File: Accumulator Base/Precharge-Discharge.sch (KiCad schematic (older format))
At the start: 17 parts, among them K1 Relay_H3FA-A-DC12, Q1 Q_NMOS_DGS, Q2 Q_NMOS_DGS, U12 DBR71210, U13 DAR71210, U15 G2RL-1-DC12., U16 G2RL-24-DC12

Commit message: Accumulator Base layout with no traces
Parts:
- removed HS1: AH50600V05000FE, symbol Mechanical:Heatsink
- added C15, C16: 100n, Capacitor_SMD:C_0805_2012Metric, symbol pspice:C
- D10, D11, D17: footprint Resistor_SMD:R_1206_3216Metric -> Diode_SMD:D_0805_2012Metric
- D5, D6: footprint (none) -> Diode_SMD:D_SMC
- K1: footprint Relay_THT:Relay_DPDT_Omron_G6SK-2 -> H3FA-A-DC12:H3FA-A
- Q1, Q2: value Q_NMOS_DGS -> Q_NMOS_GDS; footprint Package_TO_SOT_THT:TO-220-3_Horizontal_TabDown -> Package_TO_SOT_SMD:TO-252-2; symbol Device:Q_NMOS_DGS -> Device:Q_NMOS_GDS
- U15: footprint Relay_THT:Relay_SPDT_Omron-G5Q-1 -> G2RL-1_12DC:G2RL112DC
- U16: footprint Relay_THT:Relay_DPDT_Omron_G6S-2 -> G2RL-24-DC12:G2RL-24
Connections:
- net 12V: now also Q1.2 (D), Q2.2 (D); no longer Q1.1 (D), Q2.1 (D)
- net GND: now also C15.2, C16.2
- net MCU-AIR+: now also Q1.1 (G), C16.1; no longer Q1.2 (G)
- net at K1.13: now also Q2.1 (G), C15.1; no longer Q2.2 (G)
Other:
- note added: "Design by Matthew Jahnes Spring 2020\nEdited by Bert Steyaert and Sabin Zarrandikoetxea"
- note added: "Last edited 7/24/2020\n"
- note added: "Precharge, Discharge and TS_Ready signals are brought to the MCU, \nso it can be aware of the car's state"
- note added: "Precharge/Discharge Resistor\n"
- note added: "This resistor uses a headsink"
- note removed: "Design by Matthew Jahnes Spring 2020\nEdited by Bert Steyaert"
- note removed: "Discharge Resistor\n"
- note removed: "Footprints for 3 LV relays need to be double checked,\nthey were chosen wrong just for a 3D model.\n"
- note removed: "Last edited 6/23/2020\n"
- note removed: "Symbols are good, part numbers are right, footprints are wrong\n"
- moved on the sheet: D3, D4, D5, D6, D7, K1, Q1, Q2, R3, R4, R5, R6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

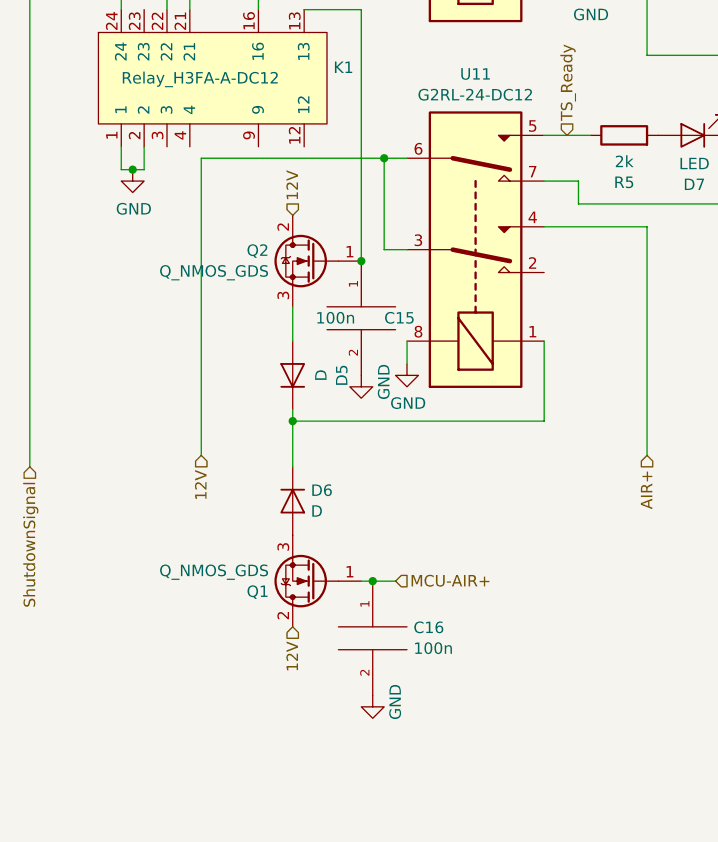
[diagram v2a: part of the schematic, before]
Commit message: fp-lib-table files unignored and pull-down resistors added on NMOS gates in Base PCB
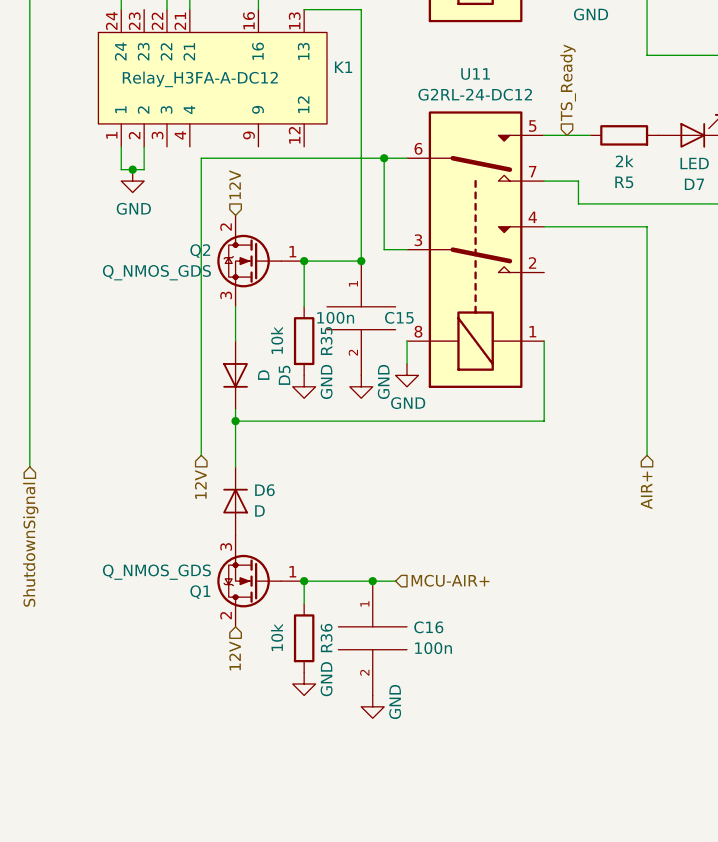
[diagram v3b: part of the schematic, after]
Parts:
- added R35, R36: 10k, Resistor_SMD:R_1206_3216Metric, symbol Device:R
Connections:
- net GND: now also R35.2, R36.2
- net MCU-AIR+: now also R36.1
- net at C15.1, K1.13, Q2.1 (G): now also R35.1
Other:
- moved on the sheet: D5, D6, Q1, Q2
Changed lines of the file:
@@
 L Device:Q_NMOS_GDS Q1
 U 1 1 5F29E655
-P 4100 6600
-F 0 "Q1" H 4304 6646 50  0000 L CNN
-F 1 "Q_NMOS_GDS" H 4304 6555 50  0000 L CNN
-F 2 "Package_TO_SOT_SMD:TO-252-2" H 4300 6700 50  0001 C CNN
-F 3 "~" H 4100 6600 50  0001 C CNN
-	1    4100 6600
+P 3850 6600
+F 0 "Q1" H 4054 6646 50  0000 L CNN
+F 1 "Q_NMOS_GDS" H 4054 6555 50  0000 L CNN
+F 2 "Package_TO_SOT_SMD:TO-252-2" H 4050 6700 50  0001 C CNN
+F 3 "~" H 3850 6600 50  0001 C CNN
+	1    3850 6600
 	-1   0    0    1
 $EndComp
@@
 L Device:Q_NMOS_GDS Q2
 U 1 1 5F2A2CC5
-P 4100 5200
-F 0 "Q2" H 4304 5246 50  0000 L CNN
-F 1 "Q_NMOS_GDS" H 4304 5155 50  0000 L CNN
-F 2 "Package_TO_SOT_SMD:TO-252-2" H 4300 5300 50  0001 C CNN
-F 3 "~" H 4100 5200 50  0001 C CNN
-	1    4100 5200
+P 3850 5200
+F 0 "Q2" H 4054 5246 50  0000 L CNN
+F 1 "Q_NMOS_GDS" H 4054 5155 50  0000 L CNN
+F 2 "Package_TO_SOT_SMD:TO-252-2" H 4050 5300 50  0001 C CNN
+F 3 "~" H 3850 5200 50  0001 C CNN
+	1    3850 5200
 	-1   0    0    -1
 $EndComp
 Wire Wire Line
 	4300 4100 4300 5200
-Text HLabel 4000 6800 3    50   Input ~ 0
+Text HLabel 3750 6800 3    50   Input ~ 0
 12V
 Wire Wire Line
@@
 Wire Wire Line
 	3600 4750 4400 4750
-Text HLabel 4000 5000 1    50   Input ~ 0
+Text HLabel 3750 5000 1    50   Input ~ 0
 12V
 Wire Wire Line
-	4000 5400 4000 5550
+	3750 5400 3750 5550
 $Comp
 L Device:D D6
 U 1 1 5F16E36E
-P 4000 6250
-F 0 "D6" V 3954 6329 50  0000 L CNN
-F 1 "D" V 4045 6329 50  0000 L CNN
-F 2 "Diode_SMD:D_SMC" H 4000 6250 50  0001 C CNN
-F 3 "~" H 4000 6250 50  0001 C CNN
-	1    4000 6250
+P 3750 6250
+F 0 "D6" V 3704 6329 50  0000 L CNN
+F 1 "D" V 3795 6329 50  0000 L CNN
+F 2 "Diode_SMD:D_SMC" H 3750 6250 50  0001 C CNN
+F 3 "~" H 3750 6250 50  0001 C CNN
+	1    3750 6250
 	0    1    1    0
 $EndComp
@@
 L Device:D D5
 U 1 1 5F158F27
-P 4000 5700
-F 0 "D5" H 4000 5484 50  0000 C CNN
-F 1 "D" H 4000 5575 50  0000 C CNN
-F 2 "Diode_SMD:D_SMC" H 4000 5700 50  0001 C CNN
-F 3 "~" H 4000 5700 50  0001 C CNN
-	1    4000 5700
+P 3750 5700
+F 0 "D5" H 3750 5484 50  0000 C CNN
+F 1 "D" H 3750 5575 50  0000 C CNN
+F 2 "Diode_SMD:D_SMC" H 3750 5700 50  0001 C CNN
+F 3 "~" H 3750 5700 50  0001 C CNN
+	1    3750 5700
 	0    -1   -1   0
 $EndComp
 Wire Wire Line
-	4000 5900 5100 5900
-Wire Wire Line
-	4000 5850 4000 5900
-Wire Wire Line
-	4000 5900 4000 6100
-Connection ~ 4000 5900
+	3750 5850 3750 5900
+Wire Wire Line
+	3750 5900 3750 6100
+Connection ~ 3750 5900
 $Comp
 L pspice:C C?
@@
 Connection ~ 4350 6600
 Wire Wire Line
-	4350 6600 4300 6600
+	4050 5200 4300 5200
 Connection ~ 4300 5200
+Wire Wire Line
+	4050 6600 4350 6600
+Wire Wire Line
+	3750 5900 5100 5900
+$Comp
+L Device:R R?
+U 1 1 5F4689FD
+P 4050 5550
+AR Path="/5E8356A3/5EC5E7BF/5F4689FD" Ref="R?"  Part="1"
+AR Path="/5F13140A/5F4689FD" Ref="R35"  Part="1"
+F 0 "R35" V 4150 5550 50  0000 C CNN
+F 1 "10k" V 3934 5550 50  0000 C CNN
+F 2 "Resistor_SMD:R_1206_3216Metric" V 3980 5550 50  0001 C CNN
+F 3 "~" H 4050 5550 50  0001 C CNN
+	1    4050 5550
+	1    0    0    -1
+$EndComp
+$Comp
+L power:GND #PWR?
+U 1 1 5F46A107
+P 4050 5700
+AR Path="/5E8356A3/5F46A107" Ref="#PWR?"  Part="1"
+AR Path="/5F46A107" Ref="#PWR?"  Part="1"
+AR Path="/5F13140A/5F46A107" Ref="#PWR0138"  Part="1"
+F 0 "#PWR0138" H 4050 5450 50  0001 C CNN
+F 1 "GND" V 4150 5750 50  0000 R CNN
+F 2 "" H 4050 5700 50  0001 C CNN
+F 3 "" H 4050 5700 50  0001 C CNN
+	1    4050 5700
+	1    0    0    -1
+$EndComp
+Wire Wire Line
+	4050 5400 4050 5200
+Connection ~ 4050 5200
+$Comp
+L Device:R R?
+U 1 1 5F46BDED
+P 4050 6850
+AR Path="/5E8356A3/5EC5E7BF/5F46BDED" Ref="R?"  Part="1"
+AR Path="/5F13140A/5F46BDED" Ref="R36"  Part="1"
+F 0 "R36" V 4150 6850 50  0000 C CNN
+F 1 "10k" V 3934 6850 50  0000 C CNN
+F 2 "Resistor_SMD:R_1206_3216Metric" V 3980 6850 50  0001 C CNN
+F 3 "~" H 4050 6850 50  0001 C CNN
+	1    4050 6850
+	1    0    0    -1
+$EndComp
+$Comp
+L power:GND #PWR?
+U 1 1 5F46D127
+P 4050 7000
+AR Path="/5E8356A3/5F46D127" Ref="#PWR?"  Part="1"
+AR Path="/5F46D127" Ref="#PWR?"  Part="1"
+AR Path="/5F13140A/5F46D127" Ref="#PWR0139"  Part="1"
+F 0 "#PWR0139" H 4050 6750 50  0001 C CNN
+F 1 "GND" V 4150 7050 50  0000 R CNN
+F 2 "" H 4050 7000 50  0001 C CNN
+F 3 "" H 4050 7000 50  0001 C CNN
+	1    4050 7000
+	1    0    0    -1
+$EndComp
+Wire Wire Line
+	4050 6700 4050 6600
+Connection ~ 4050 6600
 $EndSCHEMATC
